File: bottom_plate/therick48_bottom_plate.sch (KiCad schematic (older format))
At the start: 55 parts, among them U1 HOLE, U10 HOLE, U11 HOLE, U12 HOLE, U13 HOLE, U14 HOLE, U15 HOLE, U16 HOLE, U17 HOLE, U18 HOLE, U19 HOLE, U2 HOLE, U20 HOLE, U21 HOLE, U22 HOLE, U23 HOLE, U24 HOLE, U25 HOLE, U26 HOLE, U27 HOLE, U28 HOLE, U29 HOLE, U3 HOLE, U30 HOLE, U31 HOLE, U32 HOLE, U33 HOLE, U34 HOLE, U35 HOLE, U36 HOLE, U37 HOLE, U38 HOLE, U39 HOLE, U4 HOLE, U40 HOLE, U41 HOLE, U42 HOLE, U43 HOLE, U44 HOLE, U45 HOLE, U46 HOLE, U47 HOLE, U48 HOLE, U5 HOLE, U6 HOLE, U65 HOLE, U7 HOLE, U8 HOLE, U9 HOLE

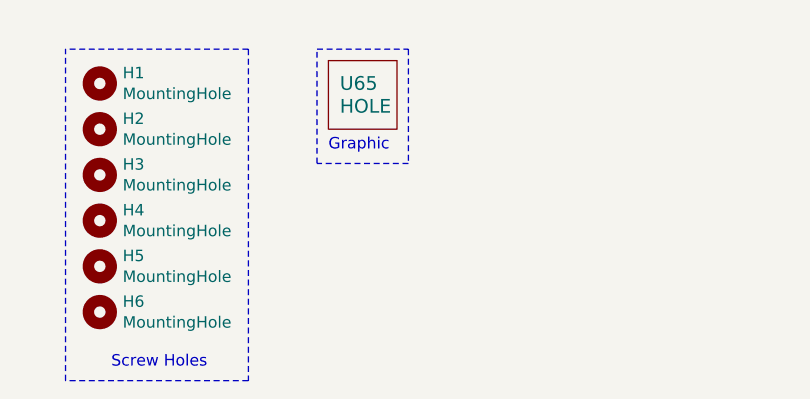
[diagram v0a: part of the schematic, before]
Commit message: Add reset hole to bottom plate
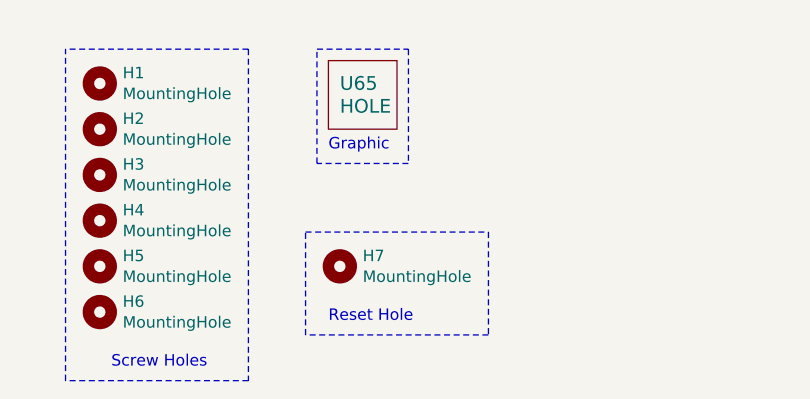
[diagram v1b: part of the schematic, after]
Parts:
- added H7: MountingHole, random-keyboard-parts:Plate_hole_4mm, symbol Mechanical:MountingHole
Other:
- note added: "Reset Hole"
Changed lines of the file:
@@
 EESchema Schematic File Version 4
-LIBS:therick64BA_19mm_bottom_plate-cache
+LIBS:therick48_bottom_plate-cache
 EELAYER 29 0
 EELAYER END
@@
 Wire Notes Line
 	1850 4400 1850 2950
+$Comp
+L Mechanical:MountingHole H7
+U 1 1 5EC2B488
+P 3050 3900
+F 0 "H7" H 3150 3946 50  0000 L CNN
+F 1 "MountingHole" H 3150 3855 50  0000 L CNN
+F 2 "random-keyboard-parts:Plate_hole_4mm" H 3050 3900 50  0001 C CNN
+F 3 "~" H 3050 3900 50  0001 C CNN
+	1    3050 3900
+	1    0    0    -1
+$EndComp
+Text Notes 3000 4150 0    50   ~ 0
+Reset Hole
+Wire Notes Line
+	3700 3750 3700 4200
+Wire Notes Line
+	3700 4200 2900 4200
+Wire Notes Line
+	2900 4200 2900 3750
+Wire Notes Line
+	2900 3750 3700 3750
 $EndSCHEMATC

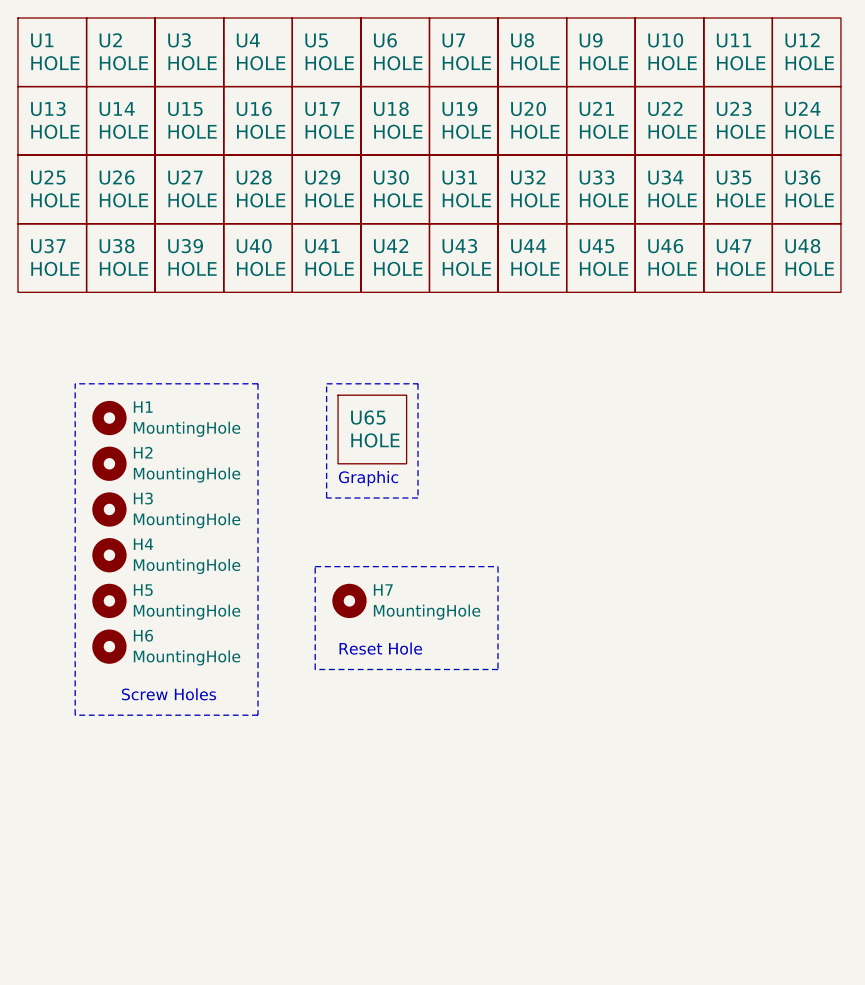
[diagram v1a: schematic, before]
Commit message: Added more mounting holes
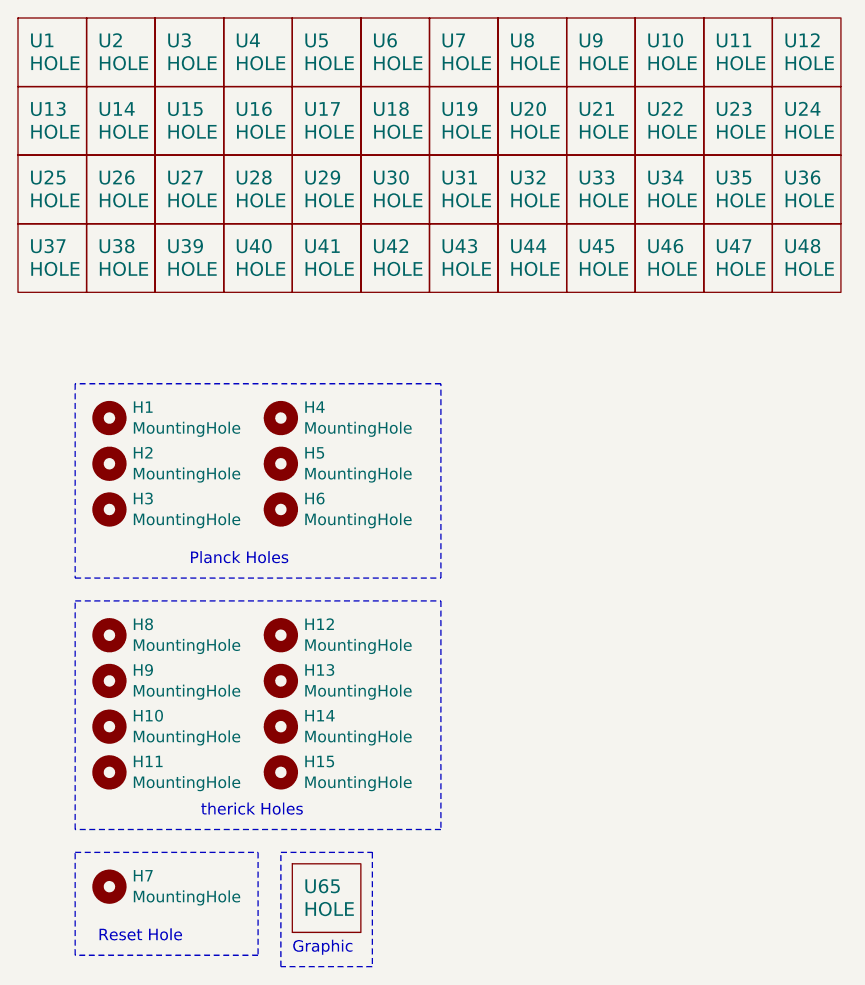
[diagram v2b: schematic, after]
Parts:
- added H10, H11, H12, H13, H14, H15, H8, H9: MountingHole, random-keyboard-parts:Generic-Mounthole, symbol Mechanical:MountingHole
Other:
- note added: "Planck Holes"
- note added: "therick Holes"
- note removed: "Screw Holes"
- moved on the sheet: H4, H5, H6, H7, U65
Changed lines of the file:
@@
 L Mechanical:MountingHole H4
 U 1 1 5DAFCFC0
-P 2000 3700
-F 0 "H4" H 2100 3746 50  0000 L CNN
-F 1 "MountingHole" H 2100 3655 50  0000 L CNN
-F 2 "random-keyboard-parts:Generic-Mounthole" H 2000 3700 50  0001 C CNN
-F 3 "~" H 2000 3700 50  0001 C CNN
-	1    2000 3700
+P 2750 3100
+F 0 "H4" H 2850 3146 50  0000 L CNN
+F 1 "MountingHole" H 2850 3055 50  0000 L CNN
+F 2 "random-keyboard-parts:Generic-Mounthole" H 2750 3100 50  0001 C CNN
+F 3 "~" H 2750 3100 50  0001 C CNN
+	1    2750 3100
 	1    0    0    -1
 $EndComp
@@
 L Mechanical:MountingHole H5
 U 1 1 5DAFD908
-P 2000 3900
-F 0 "H5" H 2100 3946 50  0000 L CNN
-F 1 "MountingHole" H 2100 3855 50  0000 L CNN
-F 2 "random-keyboard-parts:Generic-Mounthole" H 2000 3900 50  0001 C CNN
-F 3 "~" H 2000 3900 50  0001 C CNN
-	1    2000 3900
+P 2750 3300
+F 0 "H5" H 2850 3346 50  0000 L CNN
+F 1 "MountingHole" H 2850 3255 50  0000 L CNN
+F 2 "random-keyboard-parts:Generic-Mounthole" H 2750 3300 50  0001 C CNN
+F 3 "~" H 2750 3300 50  0001 C CNN
+	1    2750 3300
 	1    0    0    -1
 $EndComp
@@
 L Mechanical:MountingHole H6
 U 1 1 5DAFE1B7
-P 2000 4100
-F 0 "H6" H 2100 4146 50  0000 L CNN
-F 1 "MountingHole" H 2100 4055 50  0000 L CNN
-F 2 "random-keyboard-parts:Generic-Mounthole" H 2000 4100 50  0001 C CNN
-F 3 "~" H 2000 4100 50  0001 C CNN
-	1    2000 4100
+P 2750 3500
+F 0 "H6" H 2850 3546 50  0000 L CNN
+F 1 "MountingHole" H 2850 3455 50  0000 L CNN
+F 2 "random-keyboard-parts:Generic-Mounthole" H 2750 3500 50  0001 C CNN
+F 3 "~" H 2750 3500 50  0001 C CNN
+	1    2750 3500
 	1    0    0    -1
 $EndComp
@@
 L lets_split-cache:HOLE U65
 U 1 1 5DE56E92
-P 3150 3150
-F 0 "U65" H 3050 3200 60  0000 L CNN
-F 1 "HOLE" H 3050 3100 60  0000 L CNN
-F 2 "Artwork:rick_large" H 3150 3150 60  0001 C CNN
-F 3 "" H 3150 3150 60  0001 C CNN
-	1    3150 3150
-	1    0    0    -1
-$EndComp
-Text Notes 2050 4350 0    50   ~ 0
-Screw Holes
-Wire Notes Line
-	2650 2950 1850 2950
-Text Notes 3000 3400 0    50   ~ 0
+P 2950 5200
+F 0 "U65" H 2850 5250 60  0000 L CNN
+F 1 "HOLE" H 2850 5150 60  0000 L CNN
+F 2 "Artwork:rick_large" H 2950 5200 60  0001 C CNN
+F 3 "" H 2950 5200 60  0001 C CNN
+	1    2950 5200
+	1    0    0    -1
+$EndComp
+Text Notes 2350 3750 0    50   ~ 0
+Planck Holes
+Text Notes 2800 5450 0    50   ~ 0
 Graphic
 Wire Notes Line
-	2950 3450 2950 2950
+	2750 5500 2750 5000
 $Comp
 L lets_split-cache:HOLE U1
@@
 $EndComp
 Wire Notes Line
-	2950 2950 3350 2950
-Wire Notes Line
-	3350 2950 3350 3450
-Wire Notes Line
-	3350 3450 2950 3450
-Wire Notes Line
-	2650 2950 2650 4400
-Wire Notes Line
-	2650 4400 1850 4400
-Wire Notes Line
-	1850 4400 1850 2950
+	2750 5000 3150 5000
+Wire Notes Line
+	3150 5000 3150 5500
+Wire Notes Line
+	3150 5500 2750 5500
 $Comp
 L Mechanical:MountingHole H7
 U 1 1 5EC2B488
-P 3050 3900
-F 0 "H7" H 3150 3946 50  0000 L CNN
-F 1 "MountingHole" H 3150 3855 50  0000 L CNN
-F 2 "random-keyboard-parts:Plate_hole_4mm" H 3050 3900 50  0001 C CNN
-F 3 "~" H 3050 3900 50  0001 C CNN
-	1    3050 3900
-	1    0    0    -1
-$EndComp
-Text Notes 3000 4150 0    50   ~ 0
+P 2000 5150
+F 0 "H7" H 2100 5196 50  0000 L CNN
+F 1 "MountingHole" H 2100 5105 50  0000 L CNN
+F 2 "random-keyboard-parts:Plate_hole_4mm" H 2000 5150 50  0001 C CNN
+F 3 "~" H 2000 5150 50  0001 C CNN
+	1    2000 5150
+	1    0    0    -1
+$EndComp
+Text Notes 1950 5400 0    50   ~ 0
 Reset Hole
 Wire Notes Line
-	3700 3750 3700 4200
-Wire Notes Line
-	3700 4200 2900 4200
-Wire Notes Line
-	2900 4200 2900 3750
-Wire Notes Line
-	2900 3750 3700 3750
+	2650 5000 2650 5450
+Wire Notes Line
+	2650 5450 1850 5450
+Wire Notes Line
+	1850 5450 1850 5000
+Wire Notes Line
+	1850 5000 2650 5000
+$Comp
+L Mechanical:MountingHole H9
+U 1 1 5ED46924
+P 2000 4250
+F 0 "H9" H 2100 4296 50  0000 L CNN
+F 1 "MountingHole" H 2100 4205 50  0000 L CNN
+F 2 "random-keyboard-parts:Generic-Mounthole" H 2000 4250 50  0001 C CNN
+F 3 "~" H 2000 4250 50  0001 C CNN
+	1    2000 4250
+	1    0    0    -1
+$EndComp
+$Comp
+L Mechanical:MountingHole H8
+U 1 1 5ED4692A
+P 2000 4050
+F 0 "H8" H 2100 4096 50  0000 L CNN
+F 1 "MountingHole" H 2100 4005 50  0000 L CNN
+F 2 "random-keyboard-parts:Generic-Mounthole" H 2000 4050 50  0001 C CNN
+F 3 "~" H 2000 4050 50  0001 C CNN
+	1    2000 4050
+	1    0    0    -1
+$EndComp
+$Comp
+L Mechanical:MountingHole H10
+U 1 1 5ED46930
+P 2000 4450
+F 0 "H10" H 2100 4496 50  0000 L CNN
+F 1 "MountingHole" H 2100 4405 50  0000 L CNN
+F 2 "random-keyboard-parts:Generic-Mounthole" H 2000 4450 50  0001 C CNN
+F 3 "~" H 2000 4450 50  0001 C CNN
+	1    2000 4450
+	1    0    0    -1
+$EndComp
+$Comp
+L Mechanical:MountingHole H12
+U 1 1 5ED46936
+P 2750 4050
+F 0 "H12" H 2850 4096 50  0000 L CNN
+F 1 "MountingHole" H 2850 4005 50  0000 L CNN
+F 2 "random-keyboard-parts:Generic-Mounthole" H 2750 4050 50  0001 C CNN
+F 3 "~" H 2750 4050 50  0001 C CNN
+	1    2750 4050
+	1    0    0    -1
+$EndComp
+$Comp
+L Mechanical:MountingHole H13
+U 1 1 5ED4693C
+P 2750 4250
+F 0 "H13" H 2850 4296 50  0000 L CNN
+F 1 "MountingHole" H 2850 4205 50  0000 L CNN
+F 2 "random-keyboard-parts:Generic-Mounthole" H 2750 4250 50  0001 C CNN
+F 3 "~" H 2750 4250 50  0001 C CNN
+	1    2750 4250
+	1    0    0    -1
+$EndComp
+$Comp
+L Mechanical:MountingHole H14
+U 1 1 5ED46942
+P 2750 4450
+F 0 "H14" H 2850 4496 50  0000 L CNN
+F 1 "MountingHole" H 2850 4405 50  0000 L CNN
+F 2 "random-keyboard-parts:Generic-Mounthole" H 2750 4450 50  0001 C CNN
+F 3 "~" H 2750 4450 50  0001 C CNN
+	1    2750 4450
+	1    0    0    -1
+$EndComp
+$Comp
+L Mechanical:MountingHole H11
+U 1 1 5ED46E72
+P 2000 4650
+F 0 "H11" H 2100 4696 50  0000 L CNN
+F 1 "MountingHole" H 2100 4605 50  0000 L CNN
+F 2 "random-keyboard-parts:Generic-Mounthole" H 2000 4650 50  0001 C CNN
+F 3 "~" H 2000 4650 50  0001 C CNN
+	1    2000 4650
+	1    0    0    -1
+$EndComp
+$Comp
+L Mechanical:MountingHole H15
+U 1 1 5ED46E78
+P 2750 4650
+F 0 "H15" H 2850 4696 50  0000 L CNN
+F 1 "MountingHole" H 2850 4605 50  0000 L CNN
+F 2 "random-keyboard-parts:Generic-Mounthole" H 2750 4650 50  0001 C CNN
+F 3 "~" H 2750 4650 50  0001 C CNN
+	1    2750 4650
+	1    0    0    -1
+$EndComp
+Text Notes 2400 4850 0    50   ~ 0
+therick Holes
+Wire Notes Line
+	1850 3900 3450 3900
+Wire Notes Line
+	3450 3900 3450 4900
+Wire Notes Line
+	3450 4900 1850 4900
+Wire Notes Line
+	1850 4900 1850 3900
+Wire Notes Line
+	1850 2950 1850 3800
+Wire Notes Line
+	1850 3800 3450 3800
+Wire Notes Line
+	3450 3800 3450 2950
+Wire Notes Line
+	3450 2950 1850 2950
 $EndSCHEMATC

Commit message: Add reset hole
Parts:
- H7: footprint random-keyboard-parts:Plate_hole_4mm -> random-keyboard-parts:Generic-Mounthole
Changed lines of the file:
@@
 F 0 "H7" H 2100 5196 50  0000 L CNN
 F 1 "MountingHole" H 2100 5105 50  0000 L CNN
-F 2 "random-keyboard-parts:Plate_hole_4mm" H 2000 5150 50  0001 C CNN
+F 2 "random-keyboard-parts:Generic-Mounthole" H 2000 5150 50  0001 C CNN
 F 3 "~" H 2000 5150 50  0001 C CNN
 	1    2000 5150

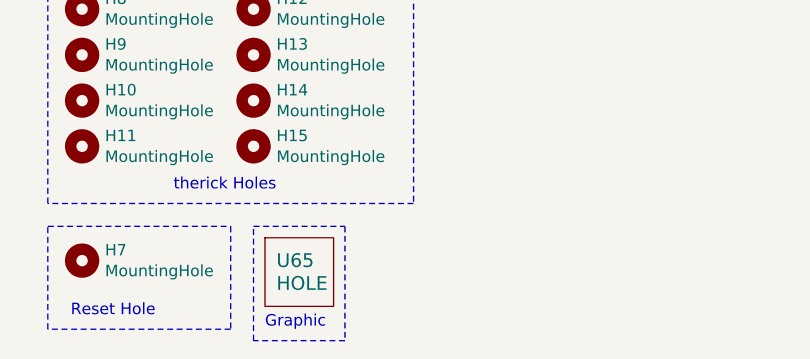
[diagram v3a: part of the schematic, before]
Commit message: Update bottom plate
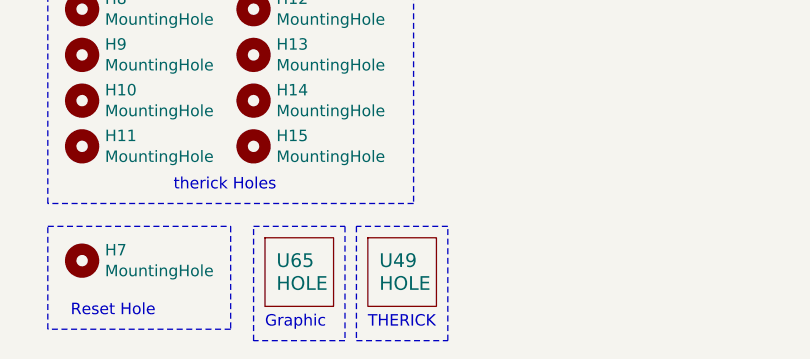
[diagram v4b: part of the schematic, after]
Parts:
- added U49: HOLE, Artwork:THERICK, symbol lets_split-cache:HOLE
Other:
- note added: "THERICK"
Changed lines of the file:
@@
 Wire Notes Line
 	3450 2950 1850 2950
+$Comp
+L lets_split-cache:HOLE U49
+U 1 1 5EF57CF7
+P 3400 5200
+F 0 "U49" H 3300 5250 60  0000 L CNN
+F 1 "HOLE" H 3300 5150 60  0000 L CNN
+F 2 "Artwork:THERICK" H 3400 5200 60  0001 C CNN
+F 3 "" H 3400 5200 60  0001 C CNN
+	1    3400 5200
+	1    0    0    -1
+$EndComp
+Text Notes 3250 5450 0    50   ~ 0
+THERICK
+Wire Notes Line
+	3200 5000 3200 5500
+Wire Notes Line
+	3200 5500 3600 5500
+Wire Notes Line
+	3600 5500 3600 5000
+Wire Notes Line
+	3600 5000 3200 5000
 $EndSCHEMATC
